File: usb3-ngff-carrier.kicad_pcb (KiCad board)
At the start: 4 copper layers, 90 x 40 mm, 62 parts, among them J1 KUSBX-BS1N9-1-BL30, J2 2199119-3, J3 Jack-DC, J5 Conn_01x03_Male, J6 SIM2070-6-1-30-00-A, J8 SIM2070-6-1-30-00-A, SW1 KMR221GLFS, U1 AP62301WU7

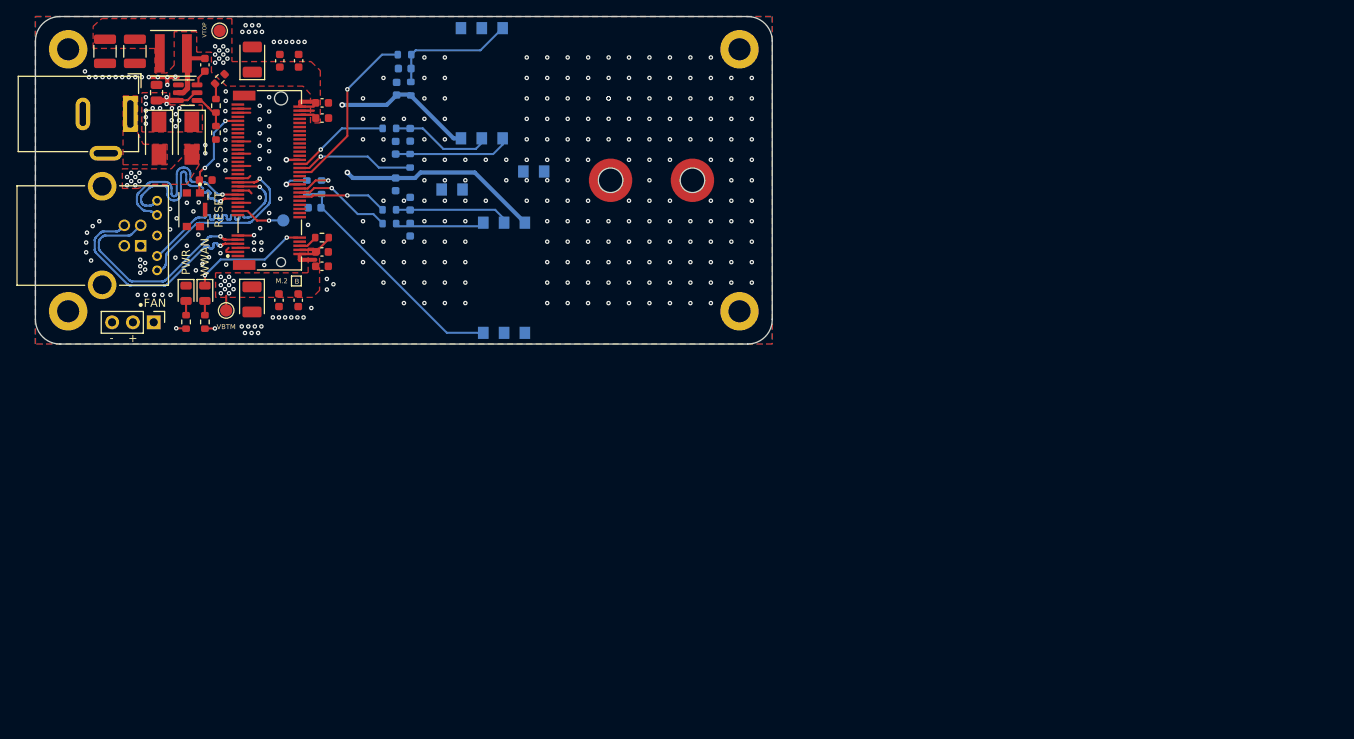
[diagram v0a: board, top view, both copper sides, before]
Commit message: feat: adds USB 2 capacitors pads for eventual assembly
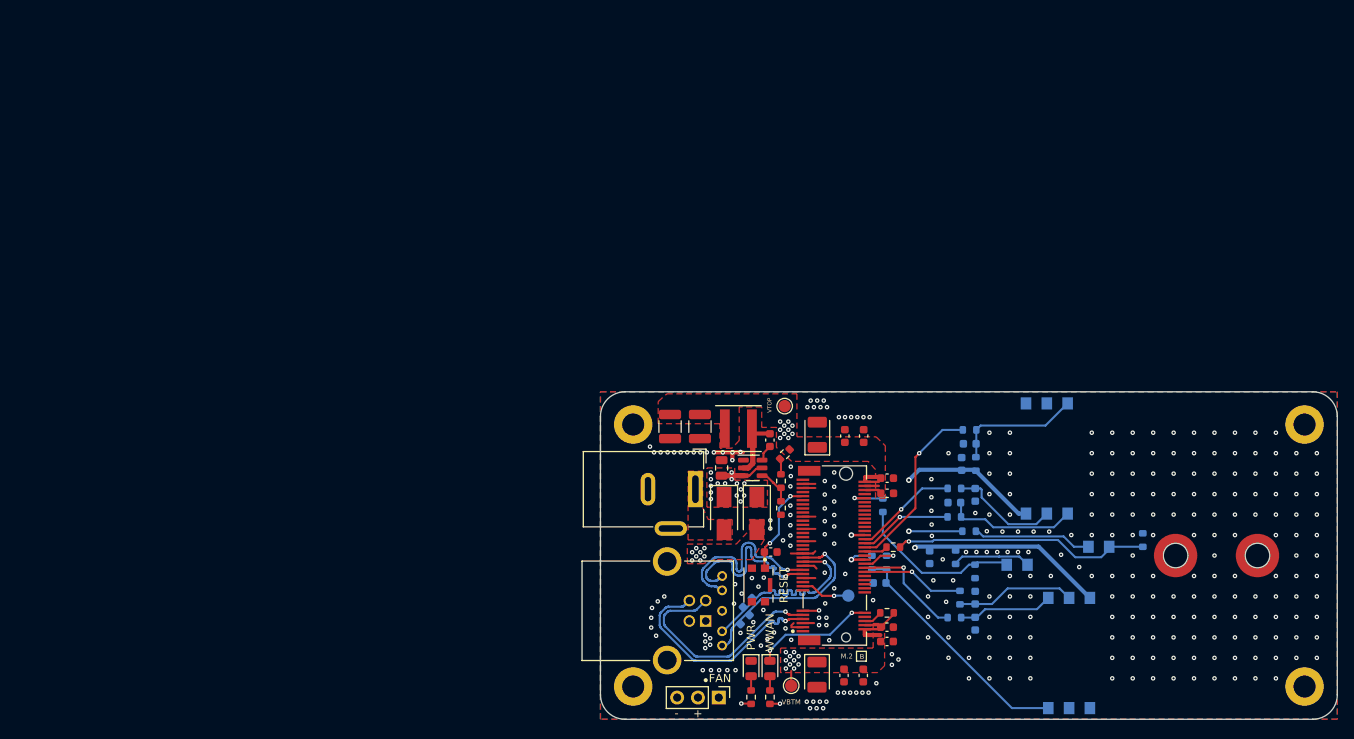
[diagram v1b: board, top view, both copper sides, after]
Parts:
- added C24: 33pF, Capacitor_SMD:C_0603_1608Metric, B.Cu at (86.7, 73.6)
- added C25: 33pF, Capacitor_SMD:C_0603_1608Metric, B.Cu at (87.0, 71.6)
- added R15: 330R, Resistor_SMD:R_0603_1608Metric, B.Cu at (112.4, 66.0)
- added R16: 10k, Resistor_SMD:R_0603_1608Metric, B.Cu at (114.8, 67.8)
- added R17: 330R, Resistor_SMD:R_0603_1608Metric, B.Cu at (114.0, 62.9)
- added R18: 10k, Resistor_SMD:R_0603_1608Metric, B.Cu at (135.3, 63.9)
- added R19: 0R, Resistor_SMD:R_0603_1608Metric, F.Cu at (104.8, 64.8)
- added R20: 0R, Resistor_SMD:R_0603_1608Metric, B.Cu at (103.5, 59.7)
- moved R10 84.3 mm to (112.9, 71.0), turned to 90 degrees
- moved C21 84.1 mm to (114.8, 71.0)
- moved C22 84.1 mm to (114.8, 74.2)
- moved R11 84.1 mm to (112.2, 73.4)
- moved C16 82.8 mm to (113.1, 54.6)
- moved R14 82.8 mm to (114.9, 54.6)
- moved C1 82.8 mm to (83.8, 55.1)
- moved C10 82.8 mm to (98.8, 80.5)
- moved C11 82.8 mm to (101.1, 80.5)
- moved C12 82.8 mm to (104.0, 76.3)
- moved C13 82.8 mm to (104.0, 74.6)
- moved C15 82.8 mm to (81.2, 50.1)
- moved C19 82.8 mm to (114.1, 52.2)
- moved C2 82.8 mm to (89.7, 51.7)
- moved C23 82.8 mm to (103.1, 69.2)
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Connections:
- J2 pad 40: unconnected-(J2-Pad40) -> Net-(J2-Pad40)
- J2 pad 66: unconnected-(J2-Pad66) -> Net-(J2-Pad66)
- J6 pad SW1: unconnected-(J6-PadSW1) -> Net-(J6-PadSW1)
- J6 pad SW2: unconnected-(J6-PadSW2) -> /USIM2_DET
- J8 pad SW1: unconnected-(J8-PadSW1) -> Net-(J8-PadSW1)
- J8 pad SW2: unconnected-(J8-PadSW2) -> /USIM1_DET
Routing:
- net /USIM2_DET: track 0.00 -> 31.6 mm, vias 0 -> 1
- net /USIM1_DET: track 0.00 -> 20.4 mm
- net Net-(J6-PadSW1): track 0.00 -> 14.3 mm
- net /USIM2_VDD: track 28.4 -> 38.6 mm, vias 2 -> 3
- net Net-(J8-PadSW1): track 0.00 -> 9.66 mm
- net Net-(J2-Pad66): track 0.00 -> 4.68 mm, vias 0 -> 1
- net /USIM2_CLK: track 14.6 -> 11.5 mm
- net Net-(J2-Pad40): track 0.00 -> 2.88 mm
- net /USIM1_RST: track 10.9 -> 12.6 mm
- net /USIM1_CLK: track 12.2 -> 13.8 mm
- net Net-(C17-Pad1): track 12.4 -> 13.3 mm
- net /USIM2_RST: track 11.9 -> 12.7 mm
- net Net-(C18-Pad1): track 15.3 -> 16.0 mm
- net GND: vias 304 -> 305
